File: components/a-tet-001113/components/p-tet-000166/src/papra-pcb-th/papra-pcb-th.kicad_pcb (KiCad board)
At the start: 2 copper layers, 45 x 65.5 mm, 40 parts, among them Q1 P-FET, Q2 N-FET, Q3 N-FET, U1 QT Py ESP32-S3

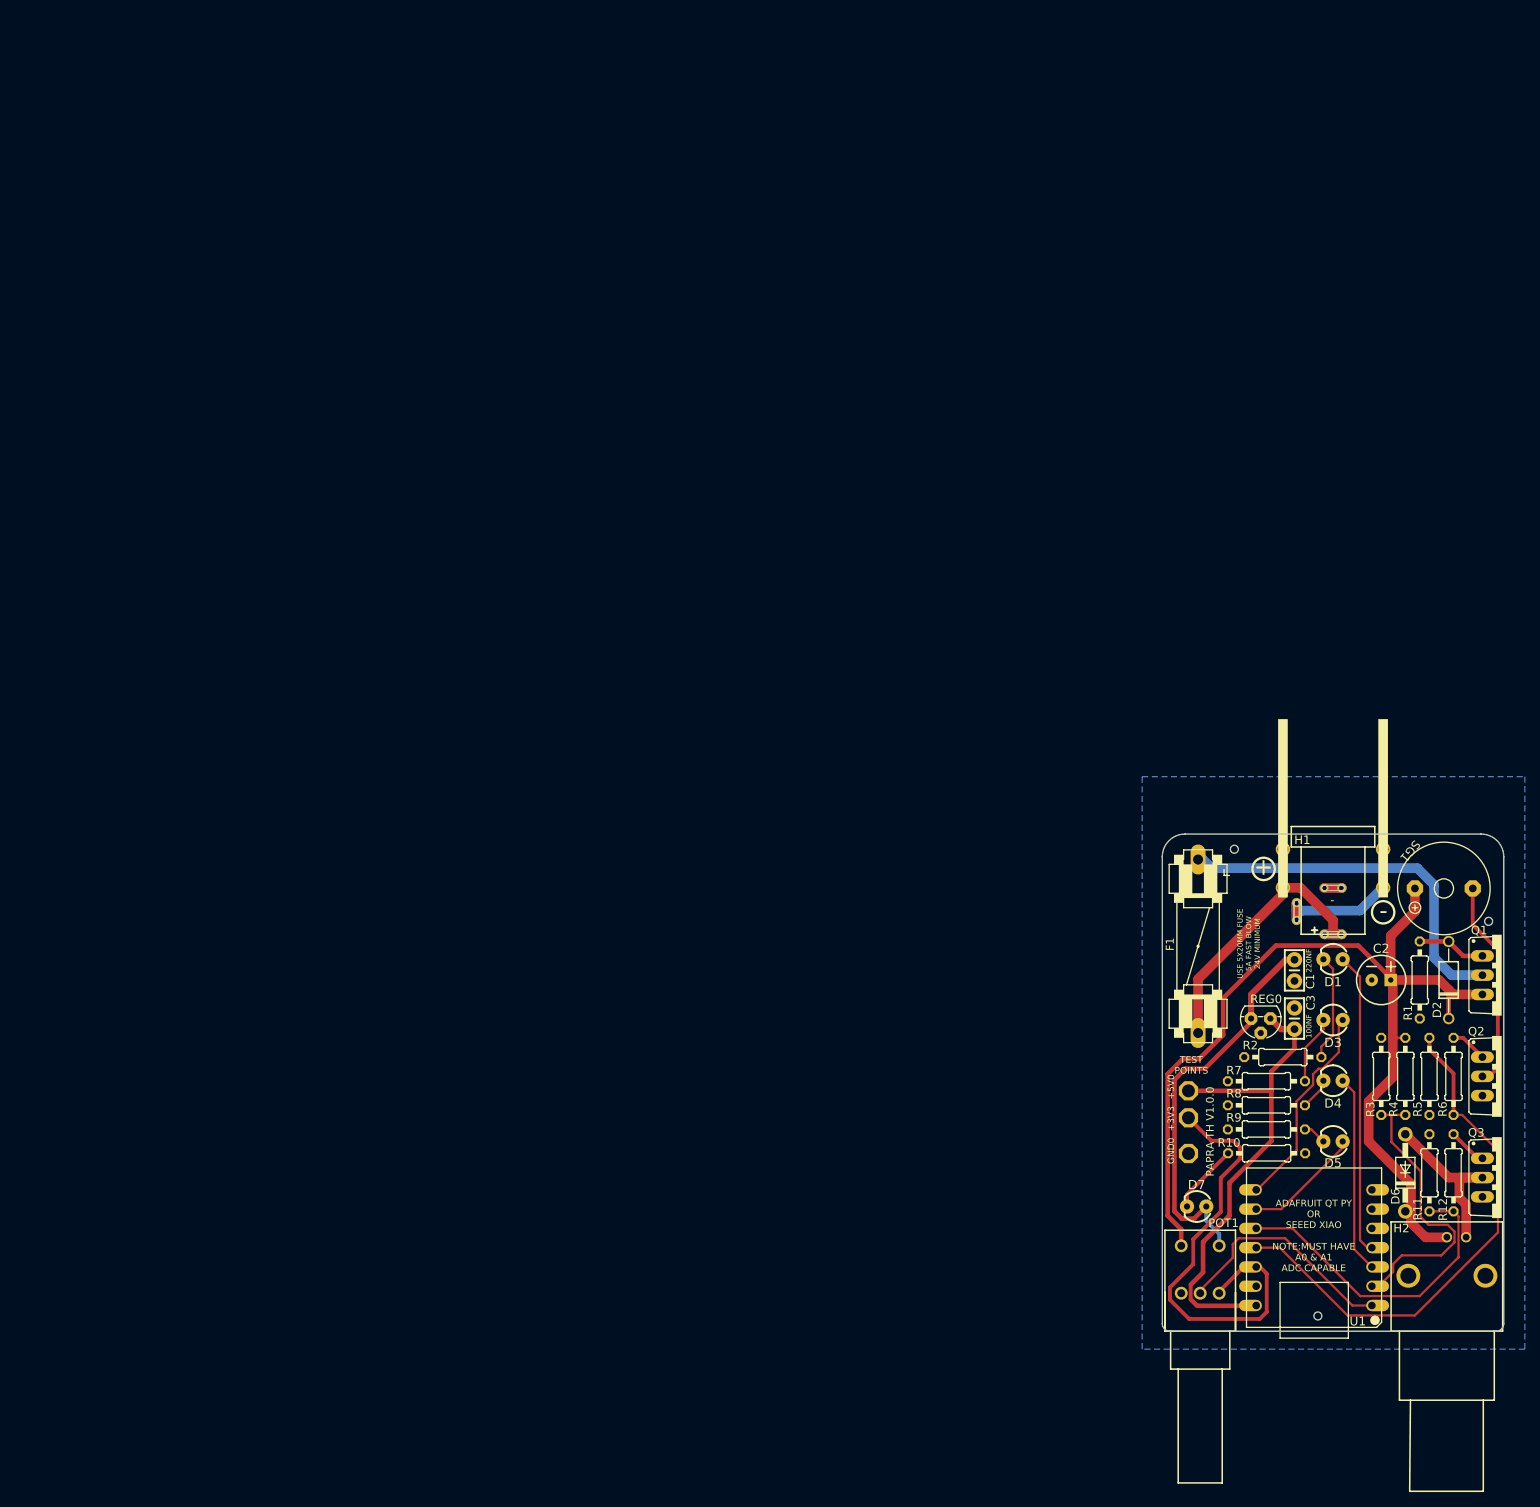
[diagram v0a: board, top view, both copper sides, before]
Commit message: finally getting this work done after work done at OC MakerFaire. Also now has tests! idk if those are helpful since the orientation of many components still required hand-based edits
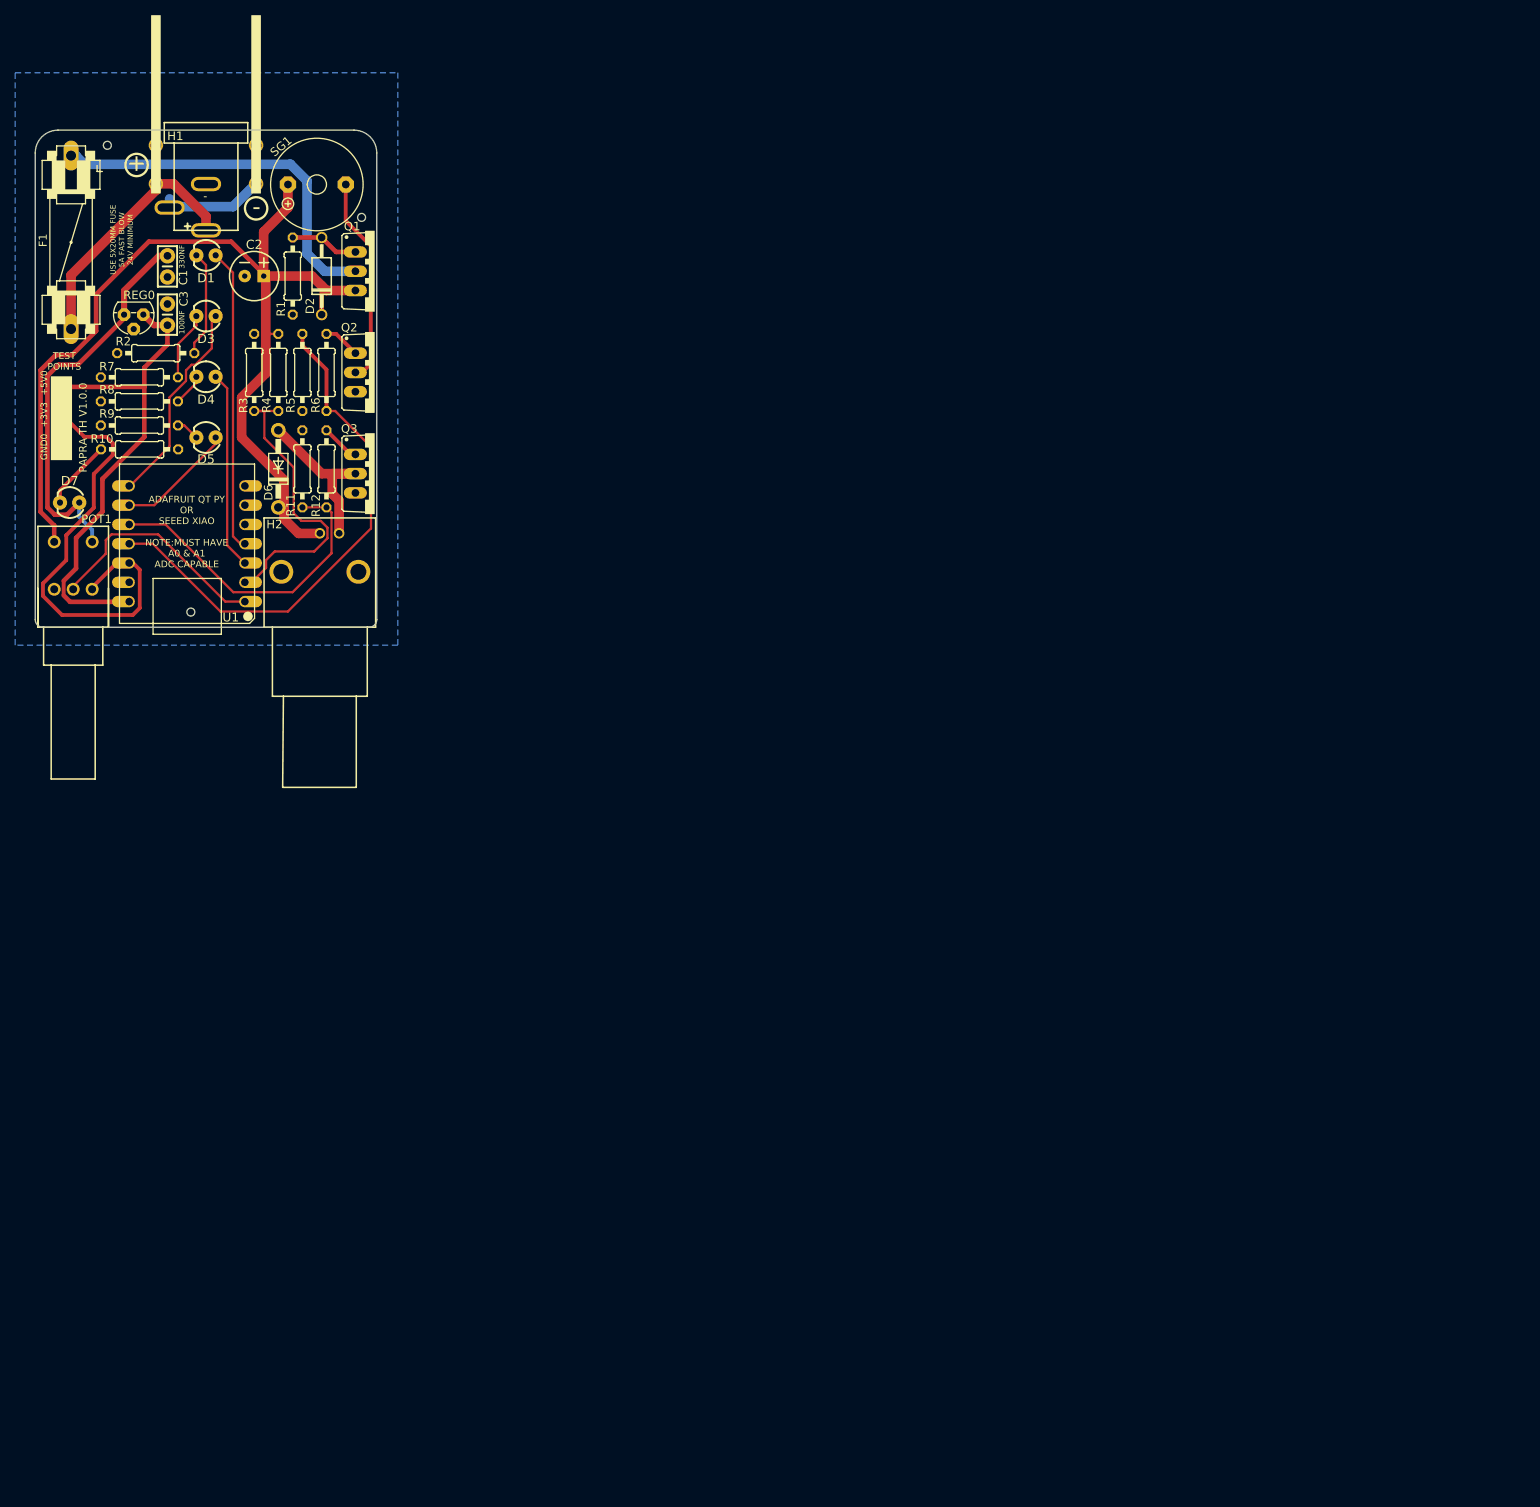
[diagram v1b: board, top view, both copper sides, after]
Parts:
- +3V3, +5V0, GND0: value PTR1PAD1-17 -> PTR1; footprint Papra TH_eagle:P1-17_385 -> papra-pcb-th:P1-17
- BATT+0, BATT-0: footprint Papra TH_eagle:TE63952-1 -> papra-pcb-th:TE63952-1
- C1, C3: footprint Papra TH_eagle:CAP-PTH-SMALL-KIT_510 -> papra-pcb-th:CAP-PTH-SMALL-KIT
- C2: footprint Papra TH_eagle:CPOL-RADIAL-2.5MM-6.5MM_510 -> papra-pcb-th:CPOL-RADIAL-2.5MM-6.5MM
- D1, D3, D4, D5, D7: footprint Papra TH_eagle:LED_3MM_529 -> papra-pcb-th:LED_3MM
- D2: footprint Papra TH_eagle:DIODE-AXIAL_30890021 -> papra-pcb-th:DIODE-AXIAL
- D6: footprint Papra TH_eagle:DO41-10_420 -> papra-pcb-th:DO41-10
- F1: footprint Papra TH_eagle:FUSE_367 -> papra-pcb-th:FUSE
- H1: footprint Papra TH_eagle:DCJACK-PJ-066A-SLOT -> papra-pcb-th:DCJACK-PJ-066A-SLOT
- H2: footprint Papra TH_eagle:TE-BNC -> papra-pcb-th:TE-BNC
- POT1: footprint Papra TH_eagle:P091S-FC20BR -> papra-pcb-th:P091S-FC20BR
- Q1: footprint Papra TH_eagle:TO220BV_30890021 -> papra-pcb-th:TO220BV
- Q2, Q3: footprint Papra TH_eagle:TO220BV_16378713 -> papra-pcb-th:TO220BV
- R1, R10, R11, R12, R2, R3, R4, R5, R6, R7, R8, R9: footprint Papra TH_eagle:0207_10_334 -> papra-pcb-th:0207_10
- REG0: value 78L05Z -> 78*; footprint Papra TH_eagle:TO92_420 -> papra-pcb-th:TO92
- SG1: footprint Papra TH_eagle:F_TMB_113 -> papra-pcb-th:F_TMB
- U1: footprint Papra TH_eagle:MODULE14P-TH+PAD -> papra-pcb-th:MODULE14P-TH+PAD
- UNK_HOLE_0: footprint Papra TH_eagle:dummyfp0 -> papra-pcb-th:dummyfp0
- UNK_HOLE_1: footprint Papra TH_eagle:dummyfp1 -> papra-pcb-th:dummyfp1
- UNK_HOLE_2: footprint Papra TH_eagle:dummyfp2 -> papra-pcb-th:dummyfp2
- moved +3V3 175.1 mm to (-19.1, 16.9)
- moved +5V0 175.1 mm to (-19.1, 13.3)
- moved BATT+0 175.1 mm to (-6.60, -16.0)
- moved BATT-0 175.1 mm to (6.60, -16.0)
- moved C1 175.1 mm to (-5.08, -2.54)
- moved D1 175.1 mm to (0.00, -4.00)
- moved D3 175.1 mm to (0.00, 4.00)
- moved D4 175.1 mm to (0.00, 12.0)
- moved D5 175.1 mm to (0.00, 20.0)
- moved D6 175.1 mm to (9.53, 24.1)
- moved F1 175.1 mm to (-17.8, -5.71)
- moved H1 175.1 mm to (0.00, -21.5)
- moved H2 175.1 mm to (15.0, 45.0)
- moved POT1 175.1 mm to (-17.5, 45.0)
- moved Q1 175.1 mm to (22.2, -1.91)
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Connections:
- net 12V-IN-FUSED renamed /12V-IN-FUSED
- net 12V-IN-GATE renamed /12V-IN-GATE
- net 12V-SWITCHED renamed /12V-SWITCHED
- net ADC-BAT renamed /ADC-BAT
- net BUZZER renamed /BUZZER
- net BUZZER-GND renamed /BUZZER-GND
- net FAN-GND renamed /FAN-GND
- net FAN-PWM renamed /FAN-PWM
- net FETGATE renamed /FETGATE
- net FETGATE1 renamed /FETGATE1
- net LED1 renamed /LED1
- net LED1.R renamed /LED1.R
- net LED2 renamed /LED2
- net LED2.R renamed /LED2.R
- net LED3 renamed /LED3
- net LED3.R renamed /LED3.R
- net LED4 renamed /LED4
- net LED4.R renamed /LED4.R
- net LED5-R renamed /LED5-R
- net POT-ADC renamed /POT-ADC
- BATT+0 pad 1: 12V-IN -> /12V-IN
- BATT+0 pad 2: 12V-IN -> /12V-IN
- BATT-0 pad 1: GND-SWITCH -> /GND-SWITCH
- BATT-0 pad 2: GND-SWITCH -> /GND-SWITCH
- F1 pad 1: 12V-IN -> /12V-IN
- H1 pad GNDBREAK: GND-SWITCH -> /GND-SWITCH
- H1 pad PWR: 12V-IN -> /12V-IN
- H2 pad P$1: (no net) -> unconnected-(H2-P3-PadP$1)
- H2 pad P$2: (no net) -> unconnected-(H2-P3-PadP$2)
- U1 pad P$5: (no net) -> unconnected-(U1-D4/A4/SDA-PadP$5)
- U1 pad P$6: (no net) -> unconnected-(U1-D5/A5/SCL-PadP$6)
- U1 pad P$7: (no net) -> unconnected-(U1-D6/A6/TX-PadP$7)
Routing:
- net 12V-IN: track 41.4 -> 0.00 mm
- net /12V-IN: track 0.00 -> 41.4 mm
- net GND-SWITCH: track 18.9 -> 0.00 mm
- net /GND-SWITCH: track 0.00 -> 18.9 mm
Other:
- board text added: "330NF"
- board text removed: "220NF"
